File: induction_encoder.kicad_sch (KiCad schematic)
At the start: 62 parts, among them J402 Conn_01x06, U1 MT9105ET, U10 IPS2200, U11 ADS1115IDGS, U12 ADS1115IDGS, U2 MT9105ET, U4 MT9105ET, U5 MT9105ET, U7 ADS1115IDGS, U8 MT9105ET

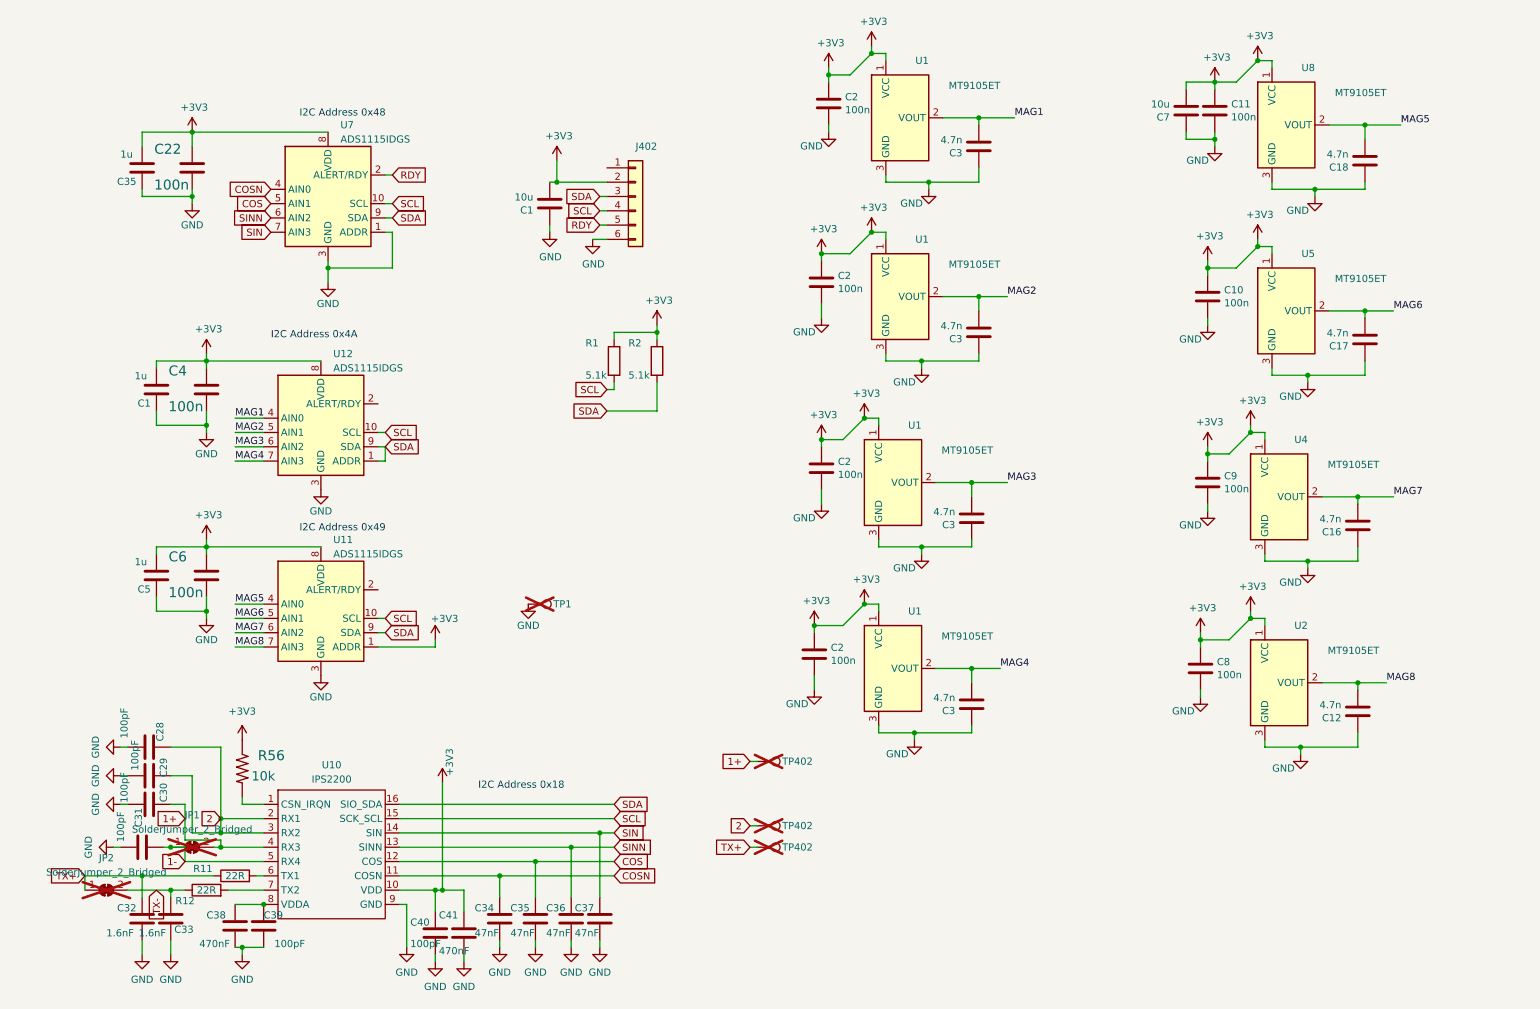
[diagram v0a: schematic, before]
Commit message: layout finished for 100-170mm induction encoder
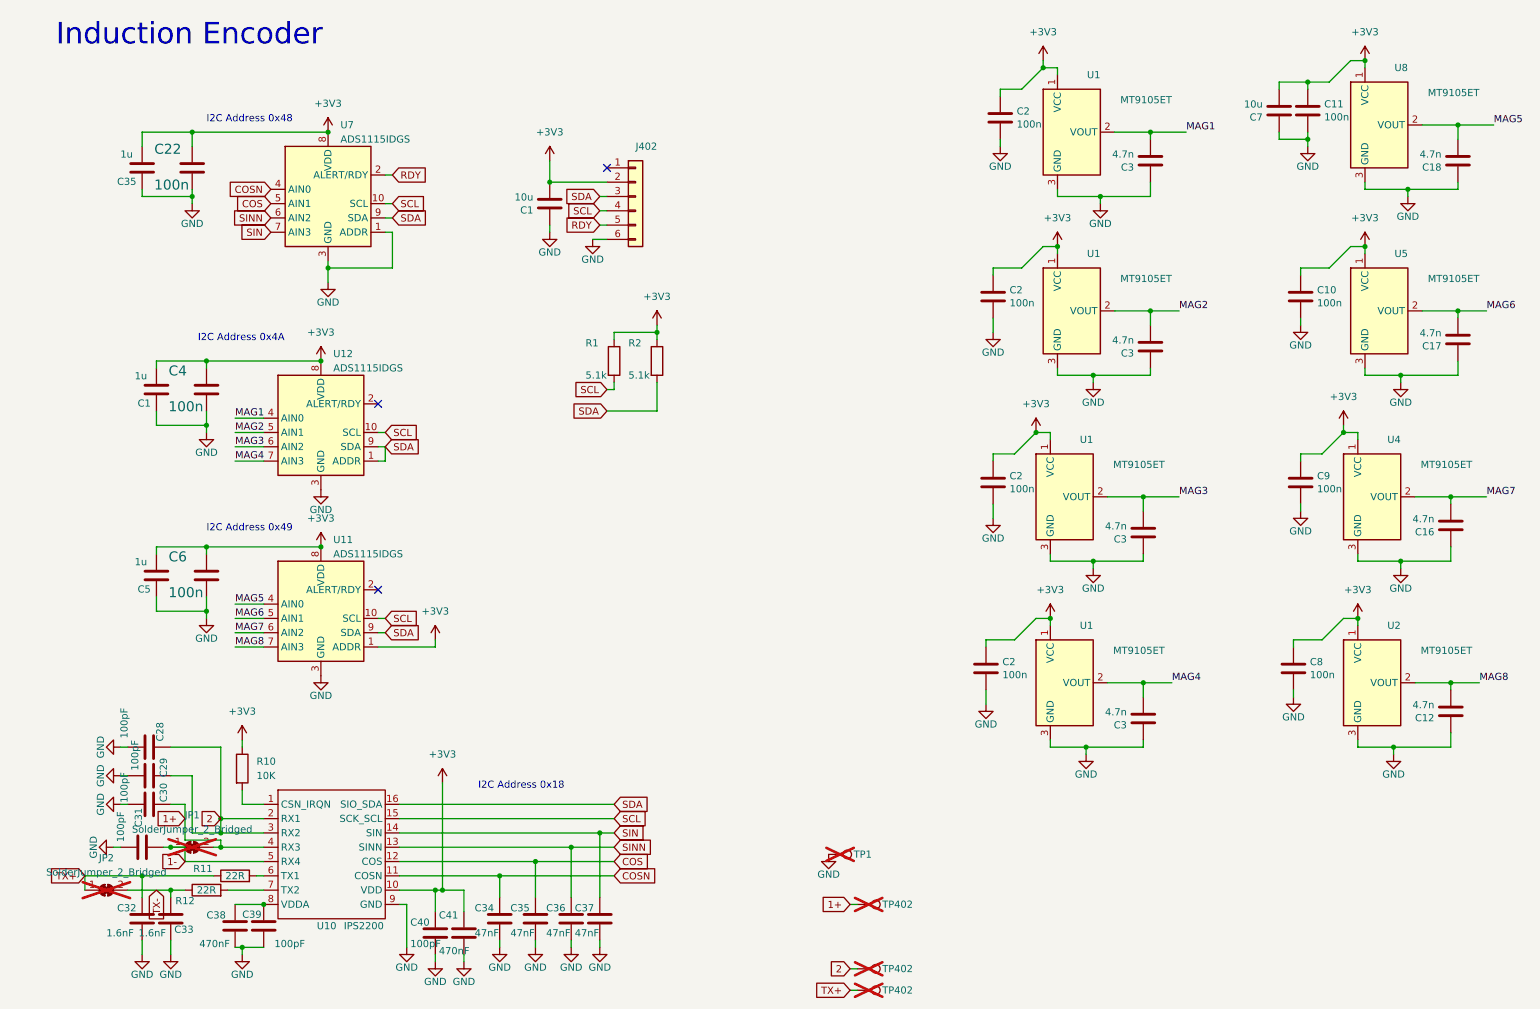
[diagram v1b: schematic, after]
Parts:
- removed R56: 10k, Resistor_SMD:R_0603_1608Metric, symbol MotorController:TAYLOR_RESISTOR
- added R10: 10K, Resistor_SMD:R_0603_1608Metric, symbol Device:R
- U10: symbol taylor_kicad:IPS2200 -> induction_encoder:IPS2200
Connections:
- net +3V3: now also R10.1
- net at U10.1 (CSN_IRQN): now also R10.2
- no-connect marks 0 -> 3
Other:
- note added: "Induction Encoder"
- company: (none) -> Rotate8
- title: (none) -> Induction Encoder
- moved on the sheet: C10, C11, C12, C16, C17, C18, C2, C3, C7, C8, C9, TP1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

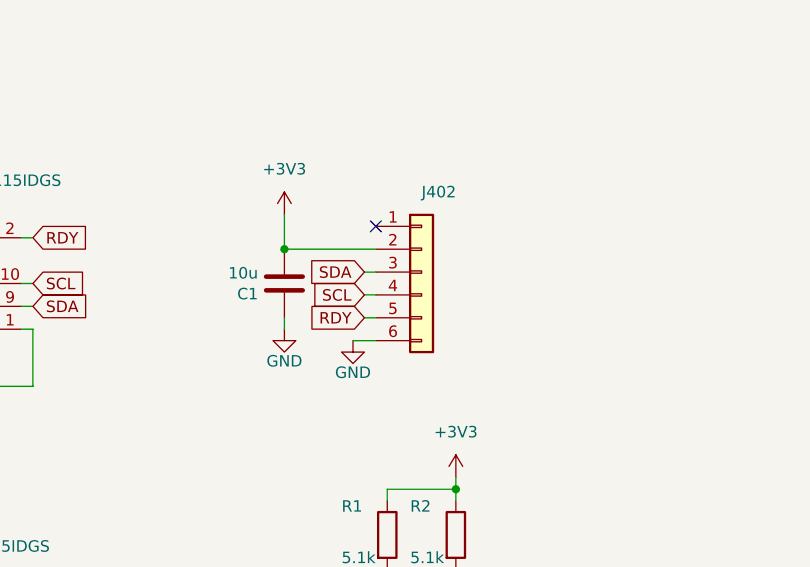
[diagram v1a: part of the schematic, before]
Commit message: 100-170mm version ordered November 2024
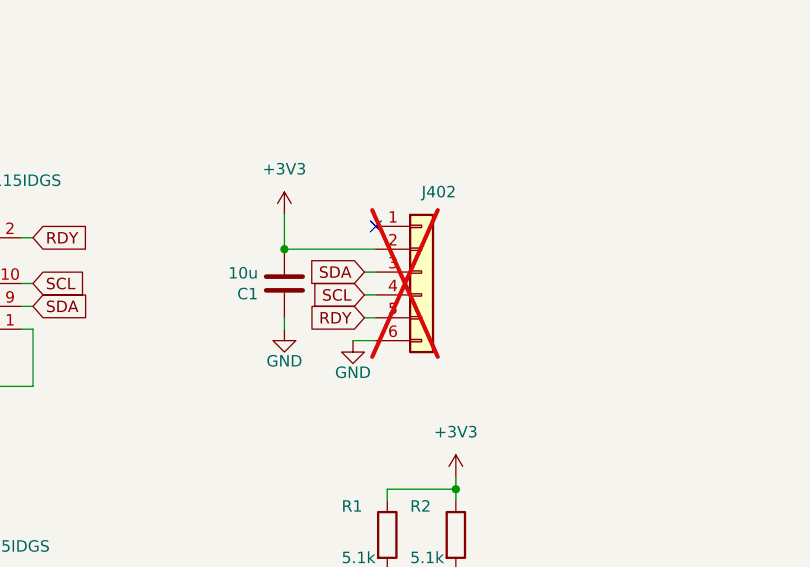
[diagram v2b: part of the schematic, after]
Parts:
- J402: now not fitted
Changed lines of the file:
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@@
 		(in_bom yes)
 		(on_board yes)
-		(dnp no)
+		(dnp yes)
 		(property "Reference" "J402"
 			(at 123.19 40.6399 0)
